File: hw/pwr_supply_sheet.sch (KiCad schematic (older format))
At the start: 12 parts

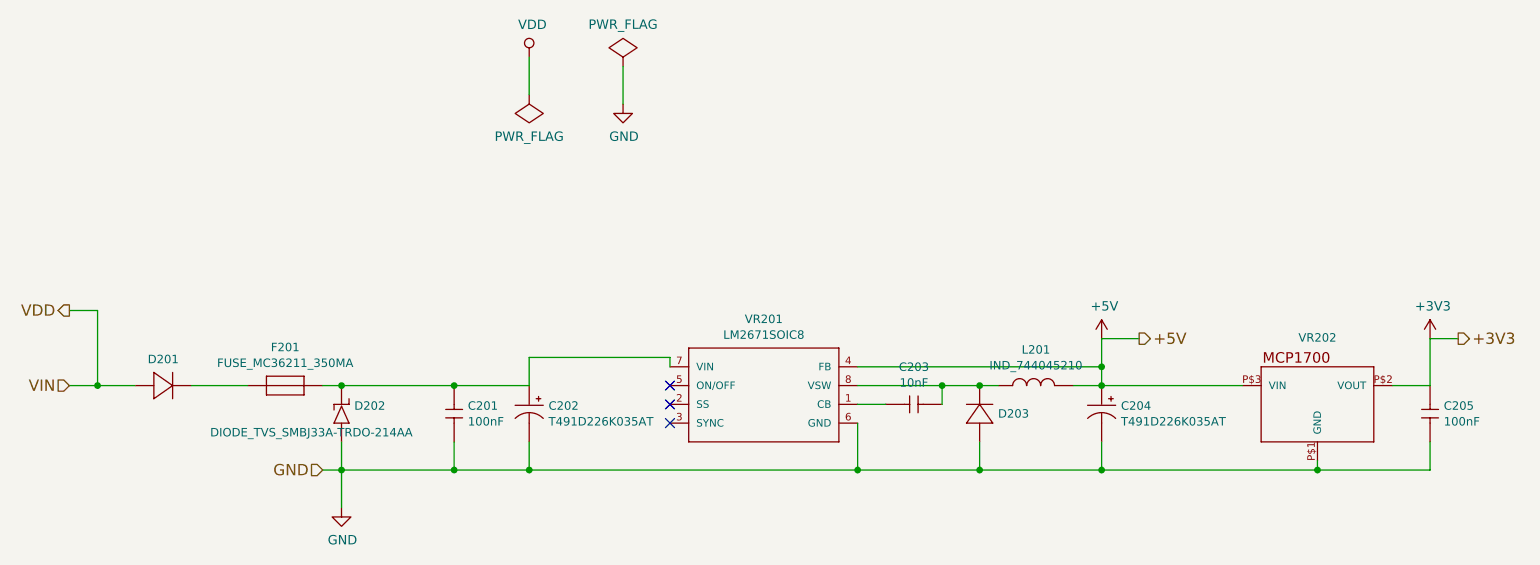
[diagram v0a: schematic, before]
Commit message: first pcb revision ready to order
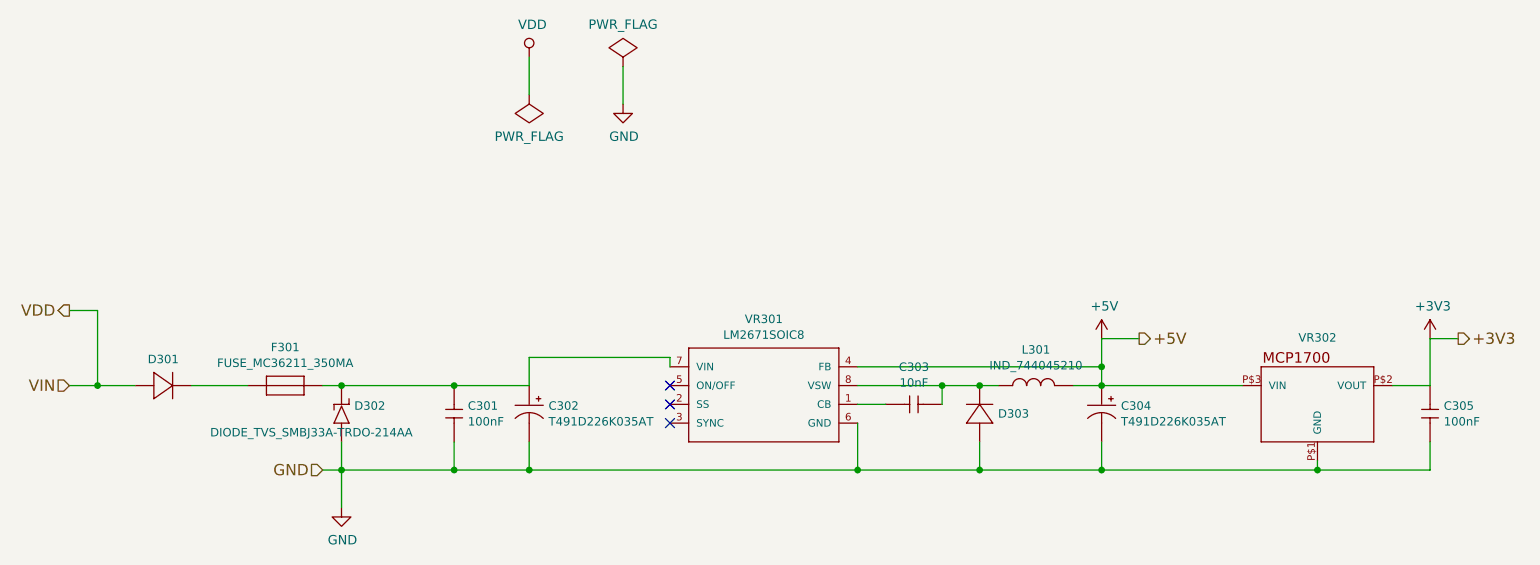
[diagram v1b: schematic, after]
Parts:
- renumbered C201 to C301, C202 to C302, C203 to C303, C204 to C304, C205 to C305, D201 to D301, D202 to D302, D203 to D303, F201 to F301, L201 to L301, VR201 to VR301, VR202 to VR302
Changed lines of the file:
@@
 LIBS:usevolt
 LIBS:wurth_elektronik_LED
+LIBS:csb-cache
 EELAYER 26 0
 EELAYER END
@@
 VIN
 $Comp
-L FUSE_MC36211_350MA F201
+L FUSE_MC36211_350MA F301
 U 1 1 57B8204F
 P 2500 3850
-F 0 "F201" H 2500 4054 45  0000 C CNN
+F 0 "F301" H 2500 4054 45  0000 C CNN
 F 1 "FUSE_MC36211_350MA" H 2500 3970 45  0000 C CNN
 F 2 "usevolt:FUSE_MC36211" H 2530 4000 20  0001 C CNN
@@
 $EndComp
 $Comp
-L DIODE_TVS_SMBJ33A-TRDO-214AA D202
+L DIODE_TVS_SMBJ33A-TRDO-214AA D302
 U 1 1 57B820C1
 P 2800 4050
-F 0 "D202" V 2892 3982 45  0000 R CNN
+F 0 "D302" V 2892 3982 45  0000 R CNN
 F 1 "DIODE_TVS_SMBJ33A-TRDO-214AA" V 2750 4750 45  0000 R CNN
 F 2 "usevolt:DO-214AA" H 2830 4200 20  0001 C CNN
@@
 $EndComp
 $Comp
-L 100nF C201
+L 100nF C301
 U 1 1 57B8217A
 P 3400 3950
-F 0 "C201" V 3408 4023 45  0000 L CNN
+F 0 "C301" V 3408 4023 45  0000 L CNN
 F 1 "100nF" V 3492 4023 45  0000 L CNN
 F 2 "kemet:0603" H 3430 4100 20  0001 C CNN
@@
 $EndComp
 $Comp
-L LM2671SOIC8 VR201
+L LM2671SOIC8 VR301
 U 1 1 57B82261
 P 4850 4150
-F 0 "VR201" H 5050 4804 45  0000 C CNN
+F 0 "VR301" H 5050 4804 45  0000 C CNN
 F 1 "LM2671SOIC8" H 5050 4720 45  0000 C CNN
 F 2 "usevolt:SOIC8" H 4880 4300 20  0001 C CNN
@@
 $EndComp
 $Comp
-L 10nF C203
+L 10nF C303
 U 1 1 57B822C5
 P 5800 3950
-F 0 "C203" H 5850 4149 45  0000 C CNN
+F 0 "C303" H 5850 4149 45  0000 C CNN
 F 1 "10nF" H 5850 4065 45  0000 C CNN
 F 2 "kemet:0603" H 5830 4100 20  0001 C CNN
@@
 $EndComp
 $Comp
-L DIODE_RS07J-GS18 D203
+L DIODE_RS07J-GS18 D303
 U 1 1 57B82329
 P 6200 3950
-F 0 "D203" V 6150 3852 45  0000 R CNN
+F 0 "D303" V 6150 3852 45  0000 R CNN
 F 1 "DIODE_RS07J-GS18" H 6220 3890 45  0001 L BNN
 F 2 "usevolt:DO219AB" H 6230 4100 20  0001 C CNN
@@
 $EndComp
 $Comp
-L REG_MCP1700 VR202
+L REG_MCP1700 VR302
 U 1 1 57B82857
 P 8000 3950
-F 0 "VR202" H 8000 4305 45  0000 C CNN
+F 0 "VR302" H 8000 4305 45  0000 C CNN
 F 1 "REG_MCP1700" H 8000 3950 45  0001 L BNN
 F 2 "usevolt:SOT-23_3-PIN" H 8030 4100 20  0001 C CNN
@@
 $EndComp
 $Comp
-L 100nF C205
+L 100nF C305
 U 1 1 57B82A3F
 P 8600 3950
-F 0 "C205" V 8608 4023 45  0000 L CNN
+F 0 "C305" V 8608 4023 45  0000 L CNN
 F 1 "100nF" V 8692 4023 45  0000 L CNN
 F 2 "kemet:0603" H 8630 4100 20  0001 C CNN
@@
 	6850 3600 6850 3850
 $Comp
-L +5V #PWR206
+L +5V #PWR014
 U 1 1 57B831F8
 P 6850 3600
-F 0 "#PWR206" H 6850 3450 50  0001 C CNN
+F 0 "#PWR014" H 6850 3450 50  0001 C CNN
 F 1 "+5V" H 6865 3773 50  0000 C CNN
 F 2 "" H 6850 3600 50  0000 C CNN
@@
 Connection ~ 6850 3750
 $Comp
-L +3V3 #PWR207
+L +3V3 #PWR015
 U 1 1 57B83259
 P 8600 3600
-F 0 "#PWR207" H 8600 3450 50  0001 C CNN
+F 0 "#PWR015" H 8600 3450 50  0001 C CNN
 F 1 "+3V3" H 8615 3773 50  0000 C CNN
 F 2 "" H 8600 3600 50  0000 C CNN
@@
 NoConn ~ 4550 4050
 $Comp
-L VDD #PWR204
+L VDD #PWR016
 U 1 1 57B9C56A
 P 3800 2100
-F 0 "#PWR204" H 3800 1950 50  0001 C CNN
+F 0 "#PWR016" H 3800 1950 50  0001 C CNN
 F 1 "VDD" H 3817 2273 50  0000 C CNN
 F 2 "" H 3800 2100 50  0000 C CNN
@@
 $EndComp
 $Comp
-L PWR_FLAG #FLG201
+L PWR_FLAG #FLG017
 U 1 1 57B9C59C
 P 3800 2300
-F 0 "#FLG201" H 3800 2395 50  0001 C CNN
+F 0 "#FLG017" H 3800 2395 50  0001 C CNN
 F 1 "PWR_FLAG" H 3800 2523 50  0000 C CNN
 F 2 "" H 3800 2300 50  0000 C CNN
@@
 	3800 2300 3800 2100
 $Comp
-L GND #PWR205
+L GND #PWR018
 U 1 1 57B9D351
 P 4300 2350
-F 0 "#PWR205" H 4300 2100 50  0001 C CNN
+F 0 "#PWR018" H 4300 2100 50  0001 C CNN
 F 1 "GND" H 4305 2177 50  0000 C CNN
 F 2 "" H 4300 2350 50  0000 C CNN
@@
 $EndComp
 $Comp
-L PWR_FLAG #FLG202
+L PWR_FLAG #FLG019
 U 1 1 57B9D3A1
 P 4300 2150
-F 0 "#FLG202" H 4300 2245 50  0001 C CNN
+F 0 "#FLG019" H 4300 2245 50  0001 C CNN
 F 1 "PWR_FLAG" H 4300 2374 50  0000 C CNN
 F 2 "" H 4300 2150 50  0000 C CNN
@@
 	4300 2150 4300 2350
 $Comp
-L GND #PWR203
+L GND #PWR020
 U 1 1 57CF1F5E
 P 2800 4500
-F 0 "#PWR203" H 2800 4250 50  0001 C CNN
+F 0 "#PWR020" H 2800 4250 50  0001 C CNN
 F 1 "GND" H 2805 4327 50  0000 C CNN
 F 2 "" H 2800 4500 50  0000 C CNN
@@
 	2700 3850 3800 3850
 $Comp
-L IND_744045210 L201
+L IND_744045210 L301
 U 1 1 58945E39
 P 6500 3850
-F 0 "L201" H 6500 4041 45  0000 C CNN
+F 0 "L301" H 6500 4041 45  0000 C CNN
 F 1 "IND_744045210" H 6500 3957 45  0000 C CNN
 F 2 "usevolt:IND_744045210" H 6530 4000 20  0001 C CNN
@@
 $EndComp
 $Comp
-L T491D226K035AT C204
+L T491D226K035AT C304
 U 1 1 58945F23
 P 6850 4050
-F 0 "C204" V 6758 4153 45  0000 L CNN
+F 0 "C304" V 6758 4153 45  0000 L CNN
 F 1 "T491D226K035AT" V 6842 4153 45  0000 L CNN
 F 2 "kemet:7343" H 6880 4200 20  0001 C CNN
@@
 $EndComp
 $Comp
-L T491D226K035AT C202
+L T491D226K035AT C302
 U 1 1 58946146
 P 3800 4050
-F 0 "C202" V 3708 4153 45  0000 L CNN
+F 0 "C302" V 3708 4153 45  0000 L CNN
 F 1 "T491D226K035AT" V 3792 4153 45  0000 L CNN
 F 2 "kemet:7343" H 3830 4200 20  0001 C CNN
@@
 	8600 4300 2700 4300
 $Comp
-L DIODE_RS07J-GS18 D201
+L DIODE_RS07J-GS18 D301
 U 1 1 5896E2A2
 P 1900 3850
-F 0 "D201" H 1850 3990 45  0000 C CNN
+F 0 "D301" H 1850 3990 45  0000 C CNN
 F 1 "DIODE_RS07J-GS18" H 1920 3790 45  0001 L BNN
 F 2 "usevolt:DO219AB" H 1930 4000 20  0001 C CNN

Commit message: starting to draw version 4.0.0
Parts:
- renumbered C301 to C201, C302 to C202, C303 to C203, C304 to C204, C305 to C205, D301 to D201, D302 to D202, D303 to D203, F301 to F201, L301 to L201, VR301 to VR201, VR302 to VR202
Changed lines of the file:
@@
 VIN
 $Comp
-L FUSE_MC36211_350MA F301
+L FUSE_MC36211_350MA F201
 U 1 1 57B8204F
 P 2500 3850
-F 0 "F301" H 2500 4054 45  0000 C CNN
+F 0 "F201" H 2500 4054 45  0000 C CNN
 F 1 "FUSE_MC36211_350MA" H 2500 3970 45  0000 C CNN
 F 2 "usevolt:FUSE_MC36211" H 2530 4000 20  0001 C CNN
@@
 $EndComp
 $Comp
-L DIODE_TVS_SMBJ33A-TRDO-214AA D302
+L DIODE_TVS_SMBJ33A-TRDO-214AA D202
 U 1 1 57B820C1
 P 2800 4050
-F 0 "D302" V 2892 3982 45  0000 R CNN
+F 0 "D202" V 2892 3982 45  0000 R CNN
 F 1 "DIODE_TVS_SMBJ33A-TRDO-214AA" V 2750 4750 45  0000 R CNN
 F 2 "usevolt:DO-214AA" H 2830 4200 20  0001 C CNN
@@
 $EndComp
 $Comp
-L 100nF C301
+L 100nF C201
 U 1 1 57B8217A
 P 3400 3950
-F 0 "C301" V 3408 4023 45  0000 L CNN
+F 0 "C201" V 3408 4023 45  0000 L CNN
 F 1 "100nF" V 3492 4023 45  0000 L CNN
 F 2 "kemet:0603" H 3430 4100 20  0001 C CNN
@@
 $EndComp
 $Comp
-L LM2671SOIC8 VR301
+L LM2671SOIC8 VR201
 U 1 1 57B82261
 P 4850 4150
-F 0 "VR301" H 5050 4804 45  0000 C CNN
+F 0 "VR201" H 5050 4804 45  0000 C CNN
 F 1 "LM2671SOIC8" H 5050 4720 45  0000 C CNN
 F 2 "usevolt:SOIC8" H 4880 4300 20  0001 C CNN
@@
 $EndComp
 $Comp
-L 10nF C303
+L 10nF C203
 U 1 1 57B822C5
 P 5800 3950
-F 0 "C303" H 5850 4149 45  0000 C CNN
+F 0 "C203" H 5850 4149 45  0000 C CNN
 F 1 "10nF" H 5850 4065 45  0000 C CNN
 F 2 "kemet:0603" H 5830 4100 20  0001 C CNN
@@
 $EndComp
 $Comp
-L DIODE_RS07J-GS18 D303
+L DIODE_RS07J-GS18 D203
 U 1 1 57B82329
 P 6200 3950
-F 0 "D303" V 6150 3852 45  0000 R CNN
+F 0 "D203" V 6150 3852 45  0000 R CNN
 F 1 "DIODE_RS07J-GS18" H 6220 3890 45  0001 L BNN
 F 2 "usevolt:DO219AB" H 6230 4100 20  0001 C CNN
@@
 $EndComp
 $Comp
-L REG_MCP1700 VR302
+L REG_MCP1700 VR202
 U 1 1 57B82857
 P 8000 3950
-F 0 "VR302" H 8000 4305 45  0000 C CNN
+F 0 "VR202" H 8000 4305 45  0000 C CNN
 F 1 "REG_MCP1700" H 8000 3950 45  0001 L BNN
 F 2 "usevolt:SOT-23_3-PIN" H 8030 4100 20  0001 C CNN
@@
 $EndComp
 $Comp
-L 100nF C305
+L 100nF C205
 U 1 1 57B82A3F
 P 8600 3950
-F 0 "C305" V 8608 4023 45  0000 L CNN
+F 0 "C205" V 8608 4023 45  0000 L CNN
 F 1 "100nF" V 8692 4023 45  0000 L CNN
 F 2 "kemet:0603" H 8630 4100 20  0001 C CNN
@@
 	2700 3850 3800 3850
 $Comp
-L IND_744045210 L301
+L IND_744045210 L201
 U 1 1 58945E39
 P 6500 3850
-F 0 "L301" H 6500 4041 45  0000 C CNN
+F 0 "L201" H 6500 4041 45  0000 C CNN
 F 1 "IND_744045210" H 6500 3957 45  0000 C CNN
 F 2 "usevolt:IND_744045210" H 6530 4000 20  0001 C CNN
@@
 $EndComp
 $Comp
-L T491D226K035AT C304
+L T491D226K035AT C204
 U 1 1 58945F23
 P 6850 4050
-F 0 "C304" V 6758 4153 45  0000 L CNN
+F 0 "C204" V 6758 4153 45  0000 L CNN
 F 1 "T491D226K035AT" V 6842 4153 45  0000 L CNN
 F 2 "kemet:7343" H 6880 4200 20  0001 C CNN
@@
 $EndComp
 $Comp
-L T491D226K035AT C302
+L T491D226K035AT C202
 U 1 1 58946146
 P 3800 4050
-F 0 "C302" V 3708 4153 45  0000 L CNN
+F 0 "C202" V 3708 4153 45  0000 L CNN
 F 1 "T491D226K035AT" V 3792 4153 45  0000 L CNN
 F 2 "kemet:7343" H 3830 4200 20  0001 C CNN
@@
 	8600 4300 2700 4300
 $Comp
-L DIODE_RS07J-GS18 D301
+L DIODE_RS07J-GS18 D201
 U 1 1 5896E2A2
 P 1900 3850
-F 0 "D301" H 1850 3990 45  0000 C CNN
+F 0 "D201" H 1850 3990 45  0000 C CNN
 F 1 "DIODE_RS07J-GS18" H 1920 3790 45  0001 L BNN
 F 2 "usevolt:DO219AB" H 1930 4000 20  0001 C CNN

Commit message: 3.1.0 hw created, not yet ordered
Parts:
- removed C202: T491D226K035AT, kemet:7343, symbol T491D226K035AT
- added C202: CAP_EEE-FK1H470P, usevolt:CAP_EEE-FK1H470P, symbol CAP_EEE-FK1H470P
- added D204, D205: SCHOTTKY_DIODE_V40PW10C, usevolt:SlimDPAK, symbol SCHOTTKY_DIODE_V40PW10C
- added D206: DIODE_TVS_TPSMD28A, usevolt:DO-214AB, symbol DIODE_TVS_TPSMD28A
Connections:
- net GND: now also C202.-, D206.1 (P)
- net VDD: now also D204.3 (CATHODE), D205.3 (CATHODE), D206.2 (N); no longer D201.P$1 (P)
- net at C201.1 (C1), D202.P$2 (N), F201.P$2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: now also C202.+
- new net VIN: D201.P$1 (P), D204.1 (A1), D204.2 (A2), D205.1 (A1), D205.2 (A2)
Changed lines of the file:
@@
 EESchema Schematic File Version 2
+LIBS:csb-rescue
 LIBS:kemet
-LIBS:multicomp
 LIBS:power
 LIBS:usevolt
 LIBS:wurth_elektronik_LED
+LIBS:yageo
 LIBS:csb-cache
 EELAYER 26 0
@@
 $Descr A4 11693 8268
 encoding utf-8
-Sheet 3 13
+Sheet 2 9
 Title "Power supply"
 Date "2016-08-20"
@@
 	0    1    1    0
 $EndComp
-Wire Wire Line
-	8000 4300 8000 4250
-Wire Wire Line
-	6850 4300 6850 4150
-Connection ~ 8000 4300
-Wire Wire Line
-	6200 4300 6200 4150
-Connection ~ 6850 4300
-Wire Wire Line
-	5550 4300 5550 4050
-Connection ~ 6200 4300
-Wire Wire Line
-	3800 4300 3800 4150
-Connection ~ 5550 4300
-Wire Wire Line
-	3400 4300 3400 4150
-Connection ~ 3800 4300
-Wire Wire Line
-	2800 4150 2800 4500
-Connection ~ 3400 4300
-Connection ~ 2800 3850
-Connection ~ 3400 3850
-Wire Wire Line
-	8600 4150 8600 4300
-Wire Wire Line
-	8600 3600 8600 3850
-Wire Wire Line
-	8600 3850 8400 3850
-Wire Wire Line
-	6700 3850 7600 3850
-Connection ~ 6850 3850
-Wire Wire Line
-	5550 3850 6300 3850
-Connection ~ 6200 3850
-Wire Wire Line
-	6000 3950 6000 3850
-Connection ~ 6000 3850
-Wire Wire Line
-	5700 3950 5550 3950
-Wire Wire Line
-	5550 3750 6850 3750
-Wire Wire Line
-	6850 3600 6850 3850
-$Comp
-L +5V #PWR204
+$Comp
+L +5V #PWR205
 U 1 1 57B831F8
 P 6850 3600
-F 0 "#PWR204" H 6850 3450 50  0001 C CNN
+F 0 "#PWR205" H 6850 3450 50  0001 C CNN
 F 1 "+5V" H 6865 3773 50  0000 C CNN
 F 2 "" H 6850 3600 50  0000 C CNN
@@
 	1    0    0    -1
 $EndComp
-Connection ~ 6850 3750
-$Comp
-L +3V3 #PWR205
+$Comp
+L +3V3 #PWR206
 U 1 1 57B83259
 P 8600 3600
-F 0 "#PWR205" H 8600 3450 50  0001 C CNN
+F 0 "#PWR206" H 8600 3450 50  0001 C CNN
 F 1 "+3V3" H 8615 3773 50  0000 C CNN
 F 2 "" H 8600 3600 50  0000 C CNN
@@
 	1    0    0    -1
 $EndComp
-Wire Wire Line
-	1350 3850 1700 3850
-Wire Wire Line
-	3800 3700 4550 3700
-Wire Wire Line
-	4550 3700 4550 3750
 Text HLabel 7050 3600 2    60   Output ~ 0
 +5V
-Wire Wire Line
-	7050 3600 6850 3600
 Text HLabel 8750 3600 2    60   Output ~ 0
 +3V3
-Wire Wire Line
-	8750 3600 8600 3600
-Text HLabel 1350 3450 0    60   Output ~ 0
+Text HLabel 3350 2850 2    60   Output ~ 0
 VDD
 Text HLabel 2700 4300 0    60   Input ~ 0
 GND
-Connection ~ 2800 4300
 NoConn ~ 4550 3850
 NoConn ~ 4550 3950
 NoConn ~ 4550 4050
 $Comp
-L VDD #PWR202
+L VDD #PWR203
 U 1 1 57B9C56A
 P 3800 2100
-F 0 "#PWR202" H 3800 1950 50  0001 C CNN
+F 0 "#PWR203" H 3800 1950 50  0001 C CNN
 F 1 "VDD" H 3817 2273 50  0000 C CNN
 F 2 "" H 3800 2100 50  0000 C CNN
@@
 	-1   0    0    1
 $EndComp
-Wire Wire Line
-	3800 2300 3800 2100
-$Comp
-L GND #PWR203
+$Comp
+L GND #PWR204
 U 1 1 57B9D351
 P 4300 2350
-F 0 "#PWR203" H 4300 2100 50  0001 C CNN
+F 0 "#PWR204" H 4300 2100 50  0001 C CNN
 F 1 "GND" H 4305 2177 50  0000 C CNN
 F 2 "" H 4300 2350 50  0000 C CNN
@@
 	1    0    0    -1
 $EndComp
-Wire Wire Line
-	4300 2150 4300 2350
 $Comp
 L GND #PWR201
@@
 	1    0    0    -1
 $EndComp
-Wire Wire Line
-	3800 3850 3800 3700
-Wire Wire Line
-	1350 3450 1500 3450
-Wire Wire Line
-	1500 3450 1500 3850
-Connection ~ 1500 3850
-Wire Wire Line
-	2700 3850 3800 3850
 $Comp
 L IND_744045210 L201
@@
 $EndComp
 $Comp
-L T491D226K035AT C202
-U 1 1 58946146
-P 3800 4050
-F 0 "C202" V 3708 4153 45  0000 L CNN
-F 1 "T491D226K035AT" V 3792 4153 45  0000 L CNN
-F 2 "kemet:7343" H 3830 4200 20  0001 C CNN
-F 3 "http://www.farnell.com/datasheets/2121523.pdf?_ga=1.259966538.1948984246.1460023966" H 3800 3990 60  0001 C CNN
-F 4 "399-8375-1-ND" H 4400 4590 60  0001 C CNN "2nd Source Part Number"
-F 5 "Farnell" H 4100 4290 60  0001 C CNN "1st Source"
-F 6 "T491D226K035AT" H 4000 4190 60  0001 C CNN "Manufacturer Part Number"
-F 7 "Digikey" H 4300 4490 60  0001 C CNN "2nd Source"
-F 8 "Kemet" H 3900 4090 60  0001 C CNN "Manufacturer"
-F 9 "1457504" H 4200 4390 60  0001 C CNN "1st Source Part Number"
-	1    3800 4050
-	0    1    1    0
-$EndComp
-Wire Wire Line
-	2000 3850 2300 3850
-Wire Wire Line
-	8600 4300 2700 4300
-$Comp
 L DIODE_RS07J-GS18 D201
 U 1 1 5896E2A2
@@
 	1    0    0    -1
 $EndComp
+$Comp
+L SCHOTTKY_DIODE_V40PW10C D204
+U 1 1 5A0333DC
+P 2050 2900
+F 0 "D204" H 2050 3247 60  0000 C CNN
+F 1 "SCHOTTKY_DIODE_V40PW10C" H 2050 3141 60  0000 C CNN
+F 2 "usevolt:SlimDPAK" H 1850 2550 60  0001 C CNN
+F 3 "http://www.farnell.com/datasheets/2245239.pdf?_ga=2.16591231.874534928.1505194133-1862443086.1504075057" H 1850 2550 60  0001 C CNN
+F 4 "2535169" H 2400 3500 60  0001 C CNN "1st Source Part Number"
+F 5 "Digikey" H 2500 3600 60  0001 C CNN "2nd Source"
+F 6 "Farnell" H 2300 3400 60  0001 C CNN "1st Source"
+F 7 "V40PW10CHM3/I" H 2200 3300 60  0001 C CNN "Manufacturer Part Number"
+F 8 "V40PW10CHM3/IGICT-ND" H 2600 3700 60  0001 C CNN "2nd Source Part Number"
+F 9 "VISHAY" H 2100 3200 60  0001 C CNN "Manufacturer"
+	1    2050 2900
+	1    0    0    -1
+$EndComp
+$Comp
+L SCHOTTKY_DIODE_V40PW10C D205
+U 1 1 5A033465
+P 2050 3350
+F 0 "D205" H 2050 3697 60  0000 C CNN
+F 1 "SCHOTTKY_DIODE_V40PW10C" H 2050 3591 60  0000 C CNN
+F 2 "usevolt:SlimDPAK" H 1850 3000 60  0001 C CNN
+F 3 "http://www.farnell.com/datasheets/2245239.pdf?_ga=2.16591231.874534928.1505194133-1862443086.1504075057" H 1850 3000 60  0001 C CNN
+F 4 "2535169" H 2400 3950 60  0001 C CNN "1st Source Part Number"
+F 5 "Digikey" H 2500 4050 60  0001 C CNN "2nd Source"
+F 6 "Farnell" H 2300 3850 60  0001 C CNN "1st Source"
+F 7 "V40PW10CHM3/I" H 2200 3750 60  0001 C CNN "Manufacturer Part Number"
+F 8 "V40PW10CHM3/IGICT-ND" H 2600 4150 60  0001 C CNN "2nd Source Part Number"
+F 9 "VISHAY" H 2100 3650 60  0001 C CNN "Manufacturer"
+	1    2050 3350
+	1    0    0    -1
+$EndComp
+Wire Wire Line
+	8000 4300 8000 4250
+Wire Wire Line
+	6850 4300 6850 4150
+Connection ~ 8000 4300
+Wire Wire Line
+	6200 4300 6200 4150
+Connection ~ 6850 4300
+Wire Wire Line
+	5550 4300 5550 4050
+Connection ~ 6200 4300
+Wire Wire Line
+	3800 4300 3800 4150
+Connection ~ 5550 4300
+Wire Wire Line
+	3400 4300 3400 4150
+Connection ~ 3800 4300
+Wire Wire Line
+	2800 4150 2800 4500
+Connection ~ 3400 4300
+Connection ~ 2800 3850
+Connection ~ 3400 3850
+Wire Wire Line
+	8600 4300 8600 4150
+Wire Wire Line
+	8600 3600 8600 3850
+Wire Wire Line
+	8600 3850 8400 3850
+Wire Wire Line
+	6700 3850 7600 3850
+Connection ~ 6850 3850
+Wire Wire Line
+	5550 3850 6300 3850
+Connection ~ 6200 3850
+Wire Wire Line
+	6000 3950 6000 3850
+Connection ~ 6000 3850
+Wire Wire Line
+	5700 3950 5550 3950
+Wire Wire Line
+	5550 3750 6850 3750
+Wire Wire Line
+	6850 3600 6850 3850
+Connection ~ 6850 3750
+Wire Wire Line
+	1350 3850 1700 3850
+Wire Wire Line
+	3800 3700 4550 3700
+Wire Wire Line
+	4550 3700 4550 3750
+Wire Wire Line
+	7050 3600 6850 3600
+Wire Wire Line
+	8750 3600 8600 3600
+Connection ~ 2800 4300
+Wire Wire Line
+	3800 2300 3800 2100
+Wire Wire Line
+	4300 2150 4300 2350
+Wire Wire Line
+	3800 3850 3800 3700
+Connection ~ 1500 3850
+Wire Wire Line
+	2700 3850 3800 3850
+Wire Wire Line
+	2000 3850 2300 3850
+Wire Wire Line
+	2700 4300 8600 4300
+Wire Wire Line
+	2450 2850 3350 2850
+Wire Wire Line
+	2800 2850 2800 3300
+Wire Wire Line
+	2800 3300 2450 3300
+Connection ~ 2800 2850
+Wire Wire Line
+	1500 2800 1500 3850
+Wire Wire Line
+	1500 2800 1650 2800
+Wire Wire Line
+	1650 2900 1500 2900
+Connection ~ 1500 2900
+Wire Wire Line
+	1650 3250 1500 3250
+Connection ~ 1500 3250
+Wire Wire Line
+	1500 3350 1650 3350
+Connection ~ 1500 3350
+$Comp
+L DIODE_TVS_TPSMD28A D206
+U 1 1 5A0E0FEE
+P 3000 3150
+F 0 "D206" V 3092 3082 45  0000 R CNN
+F 1 "DIODE_TVS_TPSMD28A" V 3008 3082 45  0000 R CNN
+F 2 "usevolt:DO-214AB" H 3030 3300 20  0001 C CNN
+F 3 "http://www.littelfuse.com/~/media/electronics/datasheets/tvs_diodes/littelfuse_tvs_diode_tpsmd_datasheet.pdf.pdf" H 3110 3160 60  0001 C CNN
+F 4 "Digi-Key" H 3410 3460 60  0001 C CNN "1st Source"
+F 5 "Littlefuse" H 3210 3260 60  0001 C CNN "Manufacturer"
+F 6 "TPSMD28A" H 3310 3360 60  0001 C CNN "Manufacturer Part Number"
+F 7 "F6570CT-ND" H 3510 3560 60  0001 C CNN "1st Source Part Number"
+	1    3000 3150
+	0    -1   -1   0
+$EndComp
+Wire Wire Line
+	3000 2950 3000 2850
+Connection ~ 3000 2850
+$Comp
+L GND #PWR202
+U 1 1 5A0E10EA
+P 3000 3350
+F 0 "#PWR202" H 3000 3100 50  0001 C CNN
+F 1 "GND" H 3005 3177 50  0000 C CNN
+F 2 "" H 3000 3350 50  0000 C CNN
+F 3 "" H 3000 3350 50  0000 C CNN
+	1    3000 3350
+	1    0    0    -1
+$EndComp
+Wire Wire Line
+	3000 3350 3000 3250
+$Comp
+L CAP_EEE-FK1H470P C202
+U 1 1 5A0E1265
+P 3800 4050
+F 0 "C202" V 3708 4153 45  0000 L CNN
+F 1 "CAP_EEE-FK1H470P" V 3792 4153 45  0000 L CNN
+F 2 "usevolt:CAP_EEE-FK1H470P" H 3830 4200 20  0001 C CNN
+F 3 "http://industrial.panasonic.com/www-cgi/jvcr13pz.cgi?E+PZ+3+ABA0120+EEEFK1H470P+7+WW" H 3800 3990 60  0001 C CNN
+F 4 "667-EEE-FK1H470P" H 4400 4590 60  0001 C CNN "2nd Source Part Number"
+F 5 "Digi-Key" H 4100 4290 60  0001 C CNN "1st Source"
+F 6 "EEE-FK1H470P" H 4000 4190 60  0001 C CNN "Manufacturer Part Number"
+F 7 "Mouser" H 4300 4490 60  0001 C CNN "2nd Source"
+F 8 "Panasonic Electronic Components" H 3900 4090 60  0001 C CNN "Manufacturer"
+F 9 "PCE3815CT-ND" H 4200 4390 60  0001 C CNN "1st Source Part Number"
+	1    3800 4050
+	0    1    1    0
+$EndComp
+Connection ~ 3800 3850
 $EndSCHEMATC
